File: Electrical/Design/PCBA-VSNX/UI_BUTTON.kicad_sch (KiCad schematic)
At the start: 10 parts, among them J901 Conn_01x05, J902 Conn_01x05

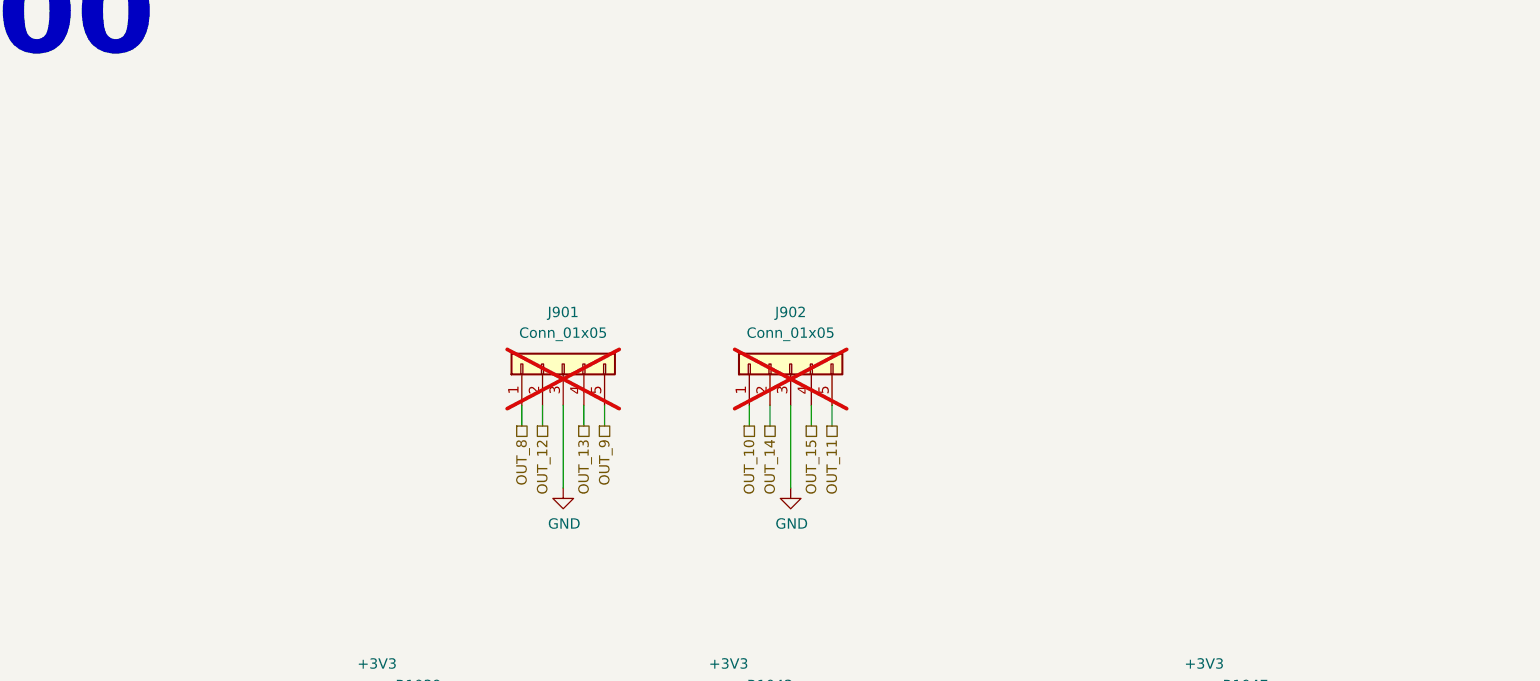
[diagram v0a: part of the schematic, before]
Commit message: SUKU VSNX buttongroup and main PCB solder connection updated
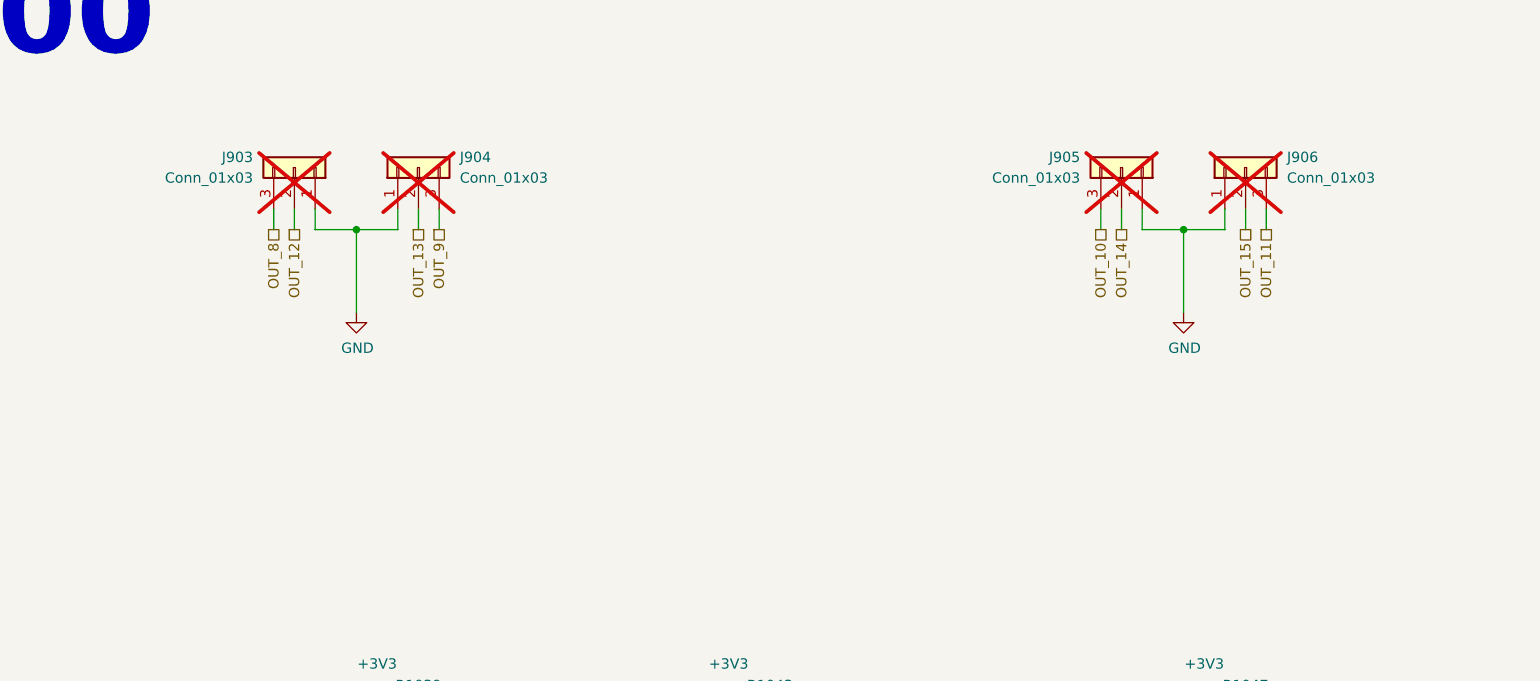
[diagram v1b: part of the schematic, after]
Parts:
- removed J901, J902: Conn_01x05, Connector_PinHeader_2.54mm:PinHeader_1x05_P2.54mm_Vertical, symbol Connector_Generic:Conn_01x05
- added J903, J904, J905, J906: Conn_01x03, suku_basics:VSNX-BUTTON-PAD, symbol Connector_Generic:Conn_01x03
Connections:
- net GND: now also J903.1 (Pin_1), J904.1 (Pin_1), J905.1 (Pin_1), J906.1 (Pin_1)
- net OUT_10: now also J905.3 (Pin_3)
- net OUT_11: now also J906.3 (Pin_3)
- net OUT_12: now also J903.2 (Pin_2)
- net OUT_13: now also J904.2 (Pin_2)
- net OUT_14: now also J905.2 (Pin_2)
- net OUT_15: now also J906.2 (Pin_2)
- net OUT_8: now also J903.3 (Pin_3)
- net OUT_9: now also J904.3 (Pin_3)

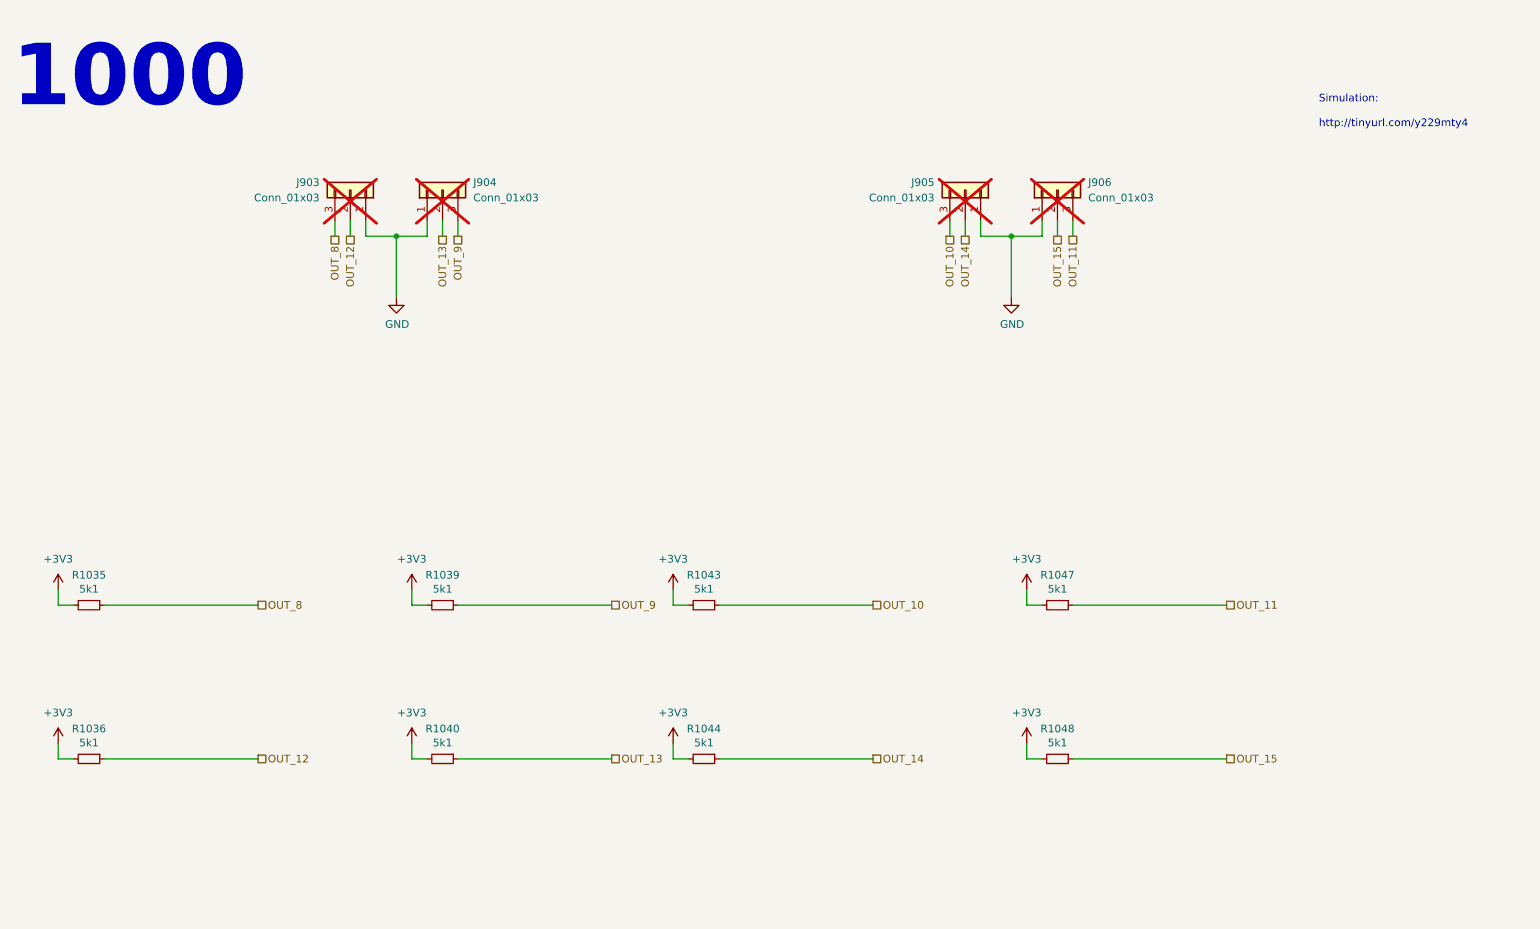
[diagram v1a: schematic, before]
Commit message: SUKU update to hall sensor based switches
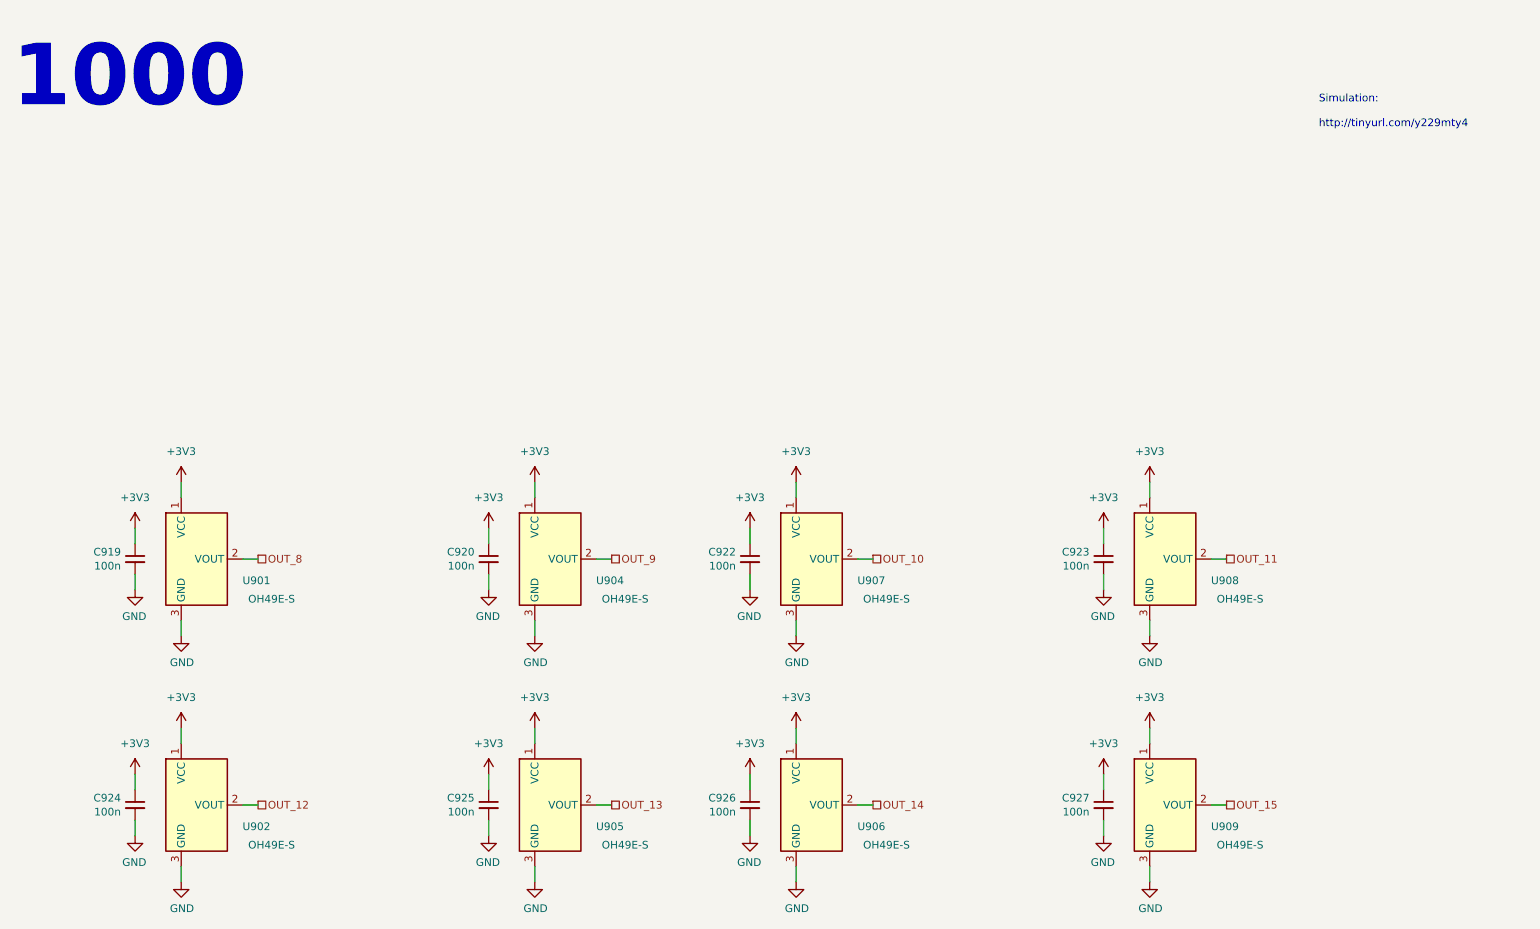
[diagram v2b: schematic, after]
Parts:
- removed J903, J904, J905, J906: Conn_01x03, suku_basics:VSNX-BUTTON-PAD, symbol Connector_Generic:Conn_01x03
- removed R1035, R1036, R1039, R1040, R1043, R1044, R1047, R1048: 5k1, suku_basics:RES_0402, symbol suku_basics:RES
- added C919, C920, C922, C923, C924, C925, C926, C927: 100n, suku_basics:CAP_0402, symbol suku_basics:CAP
- added U901, U902, U904, U905, U906, U907, U908, U909: OH49E-S, suku_basics:SOT-23W, symbol Sensor_Magnetic:A1301KLHLT-T
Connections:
- net +3V3: now also C919.1, C920.1, C922.1, C923.1, C924.1, C925.1, C926.1, C927.1, U901.1 (VCC), U902.1 (VCC), U904.1 (VCC), U905.1 (VCC), U906.1 (VCC), U907.1 (VCC), U908.1 (VCC), U909.1 (VCC)
- net GND: now also C919.2, C920.2, C922.2, C923.2, C924.2, C925.2, C926.2, C927.2, U901.3 (GND), U902.3 (GND), U904.3 (GND), U905.3 (GND), U906.3 (GND), U907.3 (GND), U908.3 (GND), U909.3 (GND)
- net OUT_10: now also U907.2 (VOUT)
- net OUT_11: now also U908.2 (VOUT)
- net OUT_12: now also U902.2 (VOUT)
- net OUT_13: now also U905.2 (VOUT)
- net OUT_14: now also U906.2 (VOUT)
- net OUT_15: now also U909.2 (VOUT)
- net OUT_8: now also U901.2 (VOUT)
- net OUT_9: now also U904.2 (VOUT)

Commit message: SUKU vsn progress to move buttons
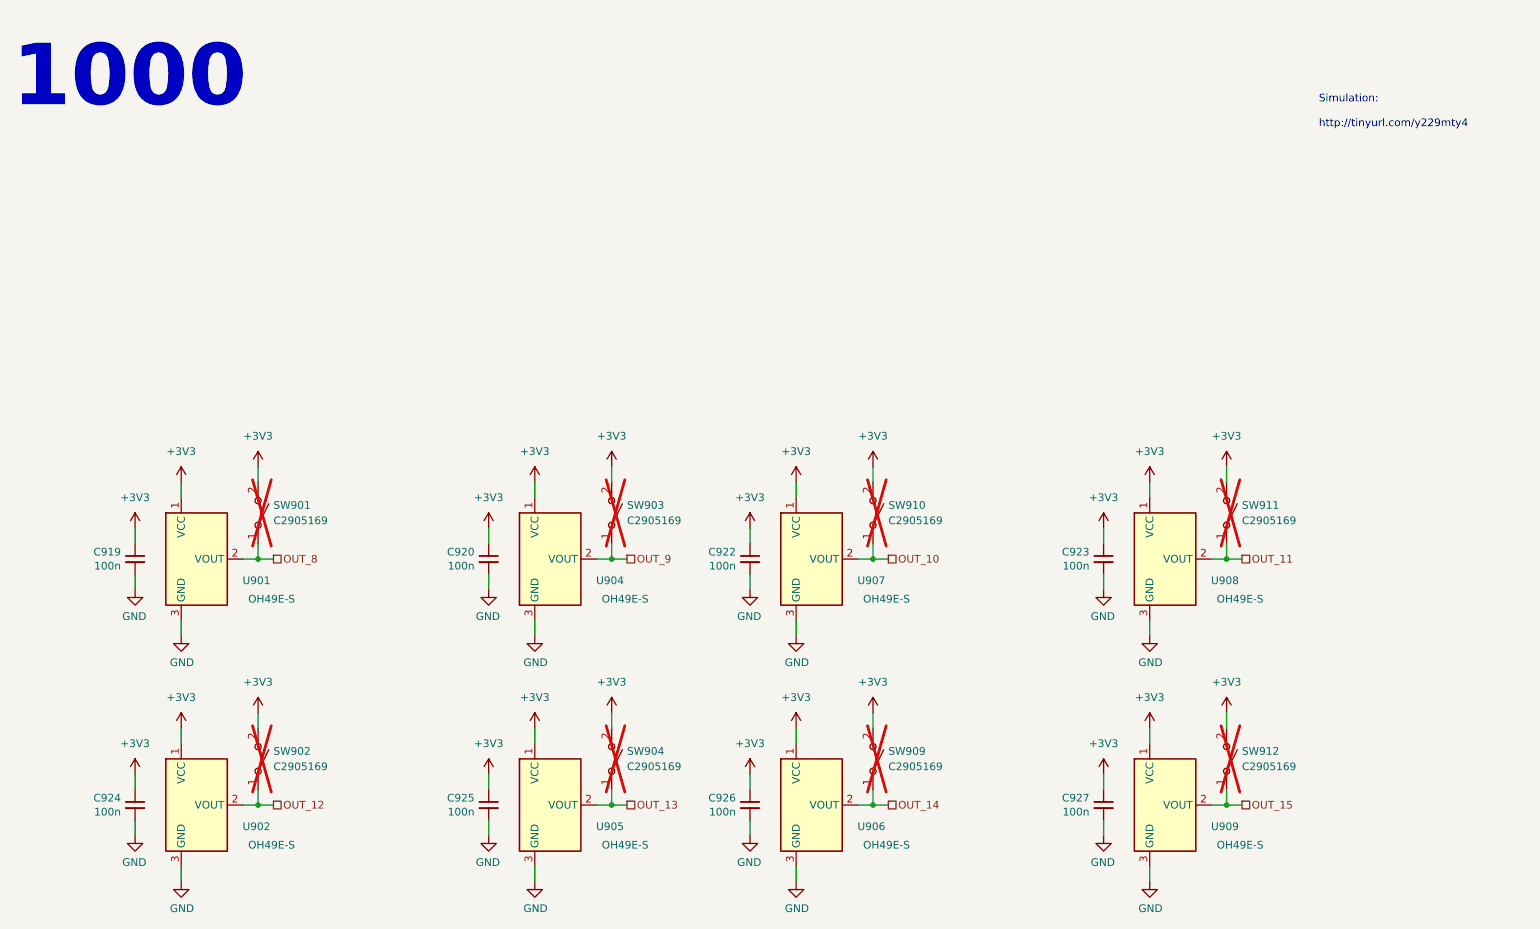
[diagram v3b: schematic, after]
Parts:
- added SW901, SW902, SW903, SW904, SW909, SW910, SW911, SW912: C2905169, suku_basics:gateron-low-profile, symbol Switch:SW_SPST
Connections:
- net +3V3: now also SW901.2 (B), SW902.2 (B), SW903.2 (B), SW904.2 (B), SW909.2 (B), SW910.2 (B), SW911.2 (B), SW912.2 (B)
- net OUT_10: now also SW910.1 (A)
- net OUT_11: now also SW911.1 (A)
- net OUT_12: now also SW902.1 (A)
- net OUT_13: now also SW904.1 (A)
- net OUT_14: now also SW909.1 (A)
- net OUT_15: now also SW912.1 (A)
- net OUT_8: now also SW901.1 (A)
- net OUT_9: now also SW903.1 (A)
